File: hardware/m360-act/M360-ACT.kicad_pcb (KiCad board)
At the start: 2 copper layers, 100 x 80 mm, 30 parts, among them J1 5V do quadro, J2 M360-RF, J3 RJ45 RELES-A, J4 RJ45 RELES-B, J5 RJ45 SENSORES, SW1 Reed, U1 AMS1117-3.3, U2 74HCT244, U3 CD74HC4067, U4 SRV05-4, U5 SRV05-4, U6 SRV05-4, U7 SRV05-4, U8 SRV05-4

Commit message: feat(hardware): legendas de serigrafia na M360-LP e na M360-ACT
Serigrafia para quem monta e liga a placa, não só para quem a projetou.

**M360-ACT** — o campo Value dos conectores passa a aparecer na serigrafia: "5V do quadro",
"M360-RF", "RJ45 RELES-A", "RJ45 RELES-B" e "RJ45 SENSORES". Sem isso o instalador vê J3, J4 e
J5 e não tem como saber qual chicote vai onde. Mais o nome do modelo abaixo da marca.

**M360-LP** — nome do modelo abaixo da marca, e **VCC/GND nas ilhas do J3**. A entrada de
alimentação é um JST de 2 vias e nada na placa dizia qual é qual; ligar invertido queima o nó,
então a legenda é proteção, não conforto. A polaridade foi conferida na netlist, não deduzida da
ordem dos pinos: pino 1 = /VIN_RAW, pino 2 = GND (mesma rede de C4.2, C6.2, J1.8, J2.8).

Três armadilhas de serigrafia, todas custaram rodada extra e ficaram registradas no README:

- **o campo Value herda a rotação do footprint.** O J1 da ACT está em rot 90, e definir só a
  posição deixou "5V do quadro" na vertical, atravessando a própria ilha do borne
  (`silk_over_copper`). É preciso forçar o ângulo;
- **afastar um rótulo de uma ilha empurrando-o para a borda troca um problema por outro.** Ao
  tirar esse mesmo texto de cima da ilha, mandei-o para x = 99 — a placa começa em x = 100, e
  entraram um `silk_edge_clearance` e dois `silk_overlap`;
- **o DRC não pega tudo.** As legendas dos RJ45 na faixa de 2,5 mm entre os TVS e os conectores
  passavam no DRC e ficavam ilegíveis sobre os corpos. Só a inspeção da imagem mostrou; subiram
  para acima da fileira de TVS.

Verificação: LP com 8 violações e ACT com 13, todas `silk_edge_clearance` das frentes dos RJ45
rente à borda — intencionais e já registradas nos commits de roteamento. **0 itens desconectados
nas duas**, ou seja, nada de elétrico foi tocado.

Co-Authored-By: Claude Opus 5 (1M context) <noreply@anthropic.com>
Claude-Session: https://claude.ai/code/session_01G3CpSsqAsoKgMUYE5MhRV7
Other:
- board text added: "M360-ACT"
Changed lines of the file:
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@@
 		)
 		(property "Value" "RJ45 RELES-B"
-			(at 0 4.89 0)
-			(layer "F.Fab")
+			(at 0 -15.34 0)
+			(layer "F.SilkS")
 			(effects
 				(font
-					(size 1 1)
+					(size 0.9 0.9)
 					(thickness 0.15)
 				)
@@
 		)
 		(property "Value" "RJ45 RELES-A"
-			(at 0 4.89 0)
-			(layer "F.Fab")
+			(at 0 -15.34 0)
+			(layer "F.SilkS")
 			(effects
 				(font
-					(size 1 1)
+					(size 0.9 0.9)
 					(thickness 0.15)
 				)
@@
 		)
 		(property "Value" "M360-RF"
-			(at -1.27 12.93 0)
-			(layer "F.Fab")
+			(at 3.2 19.58 0)
+			(layer "F.SilkS")
 			(effects
 				(font
@@
 		)
 		(property "Value" "5V do quadro"
-			(at 0 4 90)
-			(layer "F.Fab")
+			(at -7.2 0 0)
+			(layer "F.SilkS")
 			(effects
 				(font
-					(size 1 1)
+					(size 0.8 0.8)
 					(thickness 0.15)
 				)
@@
 		)
 		(property "Value" "RJ45 SENSORES"
-			(at 0 4.89 0)
-			(layer "F.Fab")
+			(at 0 -15.34 0)
+			(layer "F.SilkS")
 			(effects
 				(font
-					(size 1 1)
+					(size 0.9 0.9)
 					(thickness 0.15)
 				)
@@
 		(layer "F.SilkS")
 		(effects
+			(font
+				(size 1.5 1.5)
+				(thickness 0.25)
+			)
+		)
+	)
+	(gr_text "M360-ACT"
+		(at 176 152 0)
+		(layer "F.SilkS")
+		(effects

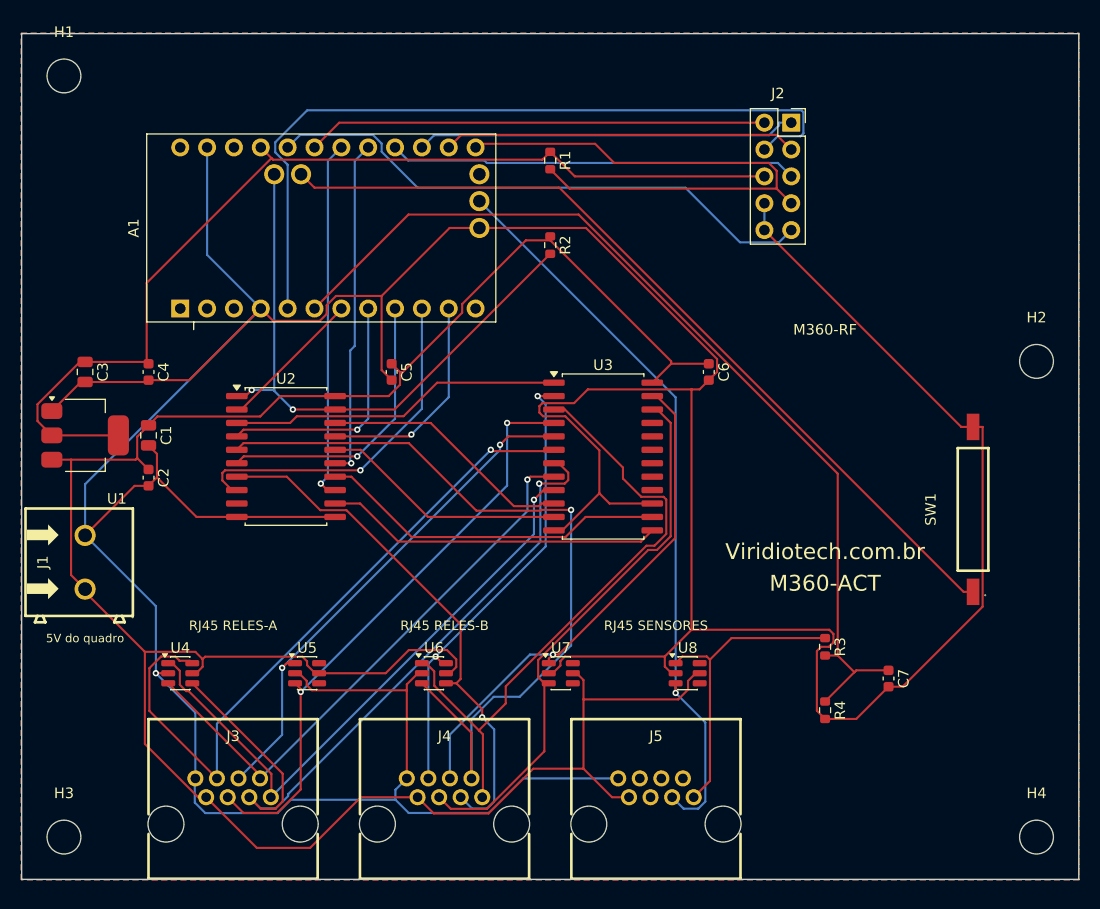
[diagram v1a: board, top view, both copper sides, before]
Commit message: feat(hardware): LP e ACT rerroteadas com o botão; GND volta a ser roteado
Conclui a troca do reed pelo botão iniciada em 0948368, que parou no esquemático.

Placas, para cada uma: del_fp.py SW1 → sincronização com o esquemático → place_*.py →
clear_tracks.py → export_dsn → dsn_sem_plano.py → Freerouting → import_ses →
zone_thermals.py → DRC com refill.

- M360-LP: 572 trilhas, 44 vias. DRC com 0 erros e 0 desconectados; restam os 8
  silk_edge_clearance dos RJ45, que já existiam.
- M360-ACT: 489 trilhas, 24 vias. DRC com 0 erros e 0 desconectados; restam os 13
  silk_edge_clearance, que já existiam. J1 em rot 0, como o place_act.py já pedia.
- Redes de todos os pads conferidas contra o HEAD: só o SW1 mudou. Trilhas todas de 0,25 mm.
- Paridade esquemático × placa com as mesmas contagens da base (237 e 195); some o
  footprint_symbol_mismatch do SW1.

**O GND não era roteado — e era isso que partia o plano.** Com zona de GND na placa, o DSN
declara `plane GND` e o Freerouting não desenha um fio de terra sequer. O primeiro roteamento
(bf701dc, 88 segmentos de GND) foi feito antes de as zonas existirem; todo rerroteamento
posterior perdia esse terra. Rerroteada com o DSN como sai do KiCad, a LP deu 16
unconnected_items, todos "Zona [GND]"; tirando as declarações plane, 0 — 100 segmentos de GND
na LP e 95 na ACT. Explica também os 15 desconectados imóveis da sessão anterior (§11.6).
Novo `tools/dsn_sem_plano.py`, e a §11 corrigida: 11.2, 11.4, 11.5 e 11.6.

Ajustes que o DRC pediu depois do rerroteamento:
- J4 da ACT, pino 8: starved_thermal → ligação sólida (pad_zone_connect.py), como o J3;
- silk_lp.py: referência do SW1 saía sobre "M360-LP"; vai para (172, 155);
- silk_act.py: referência do U1 encostava no J1, agora em rot 0; sobe para y = 143.

Botão: SHOU HAN TS665CJ, C393938, tátil 6 × 6 mm THT, SW1 nas três placas (LP, ACT e GW),
**solda manual e fora do PCBA**. Propriedade LCSC gravada nos três esquemáticos, com netlists
idênticas antes e depois. `add_lcsc.py` g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
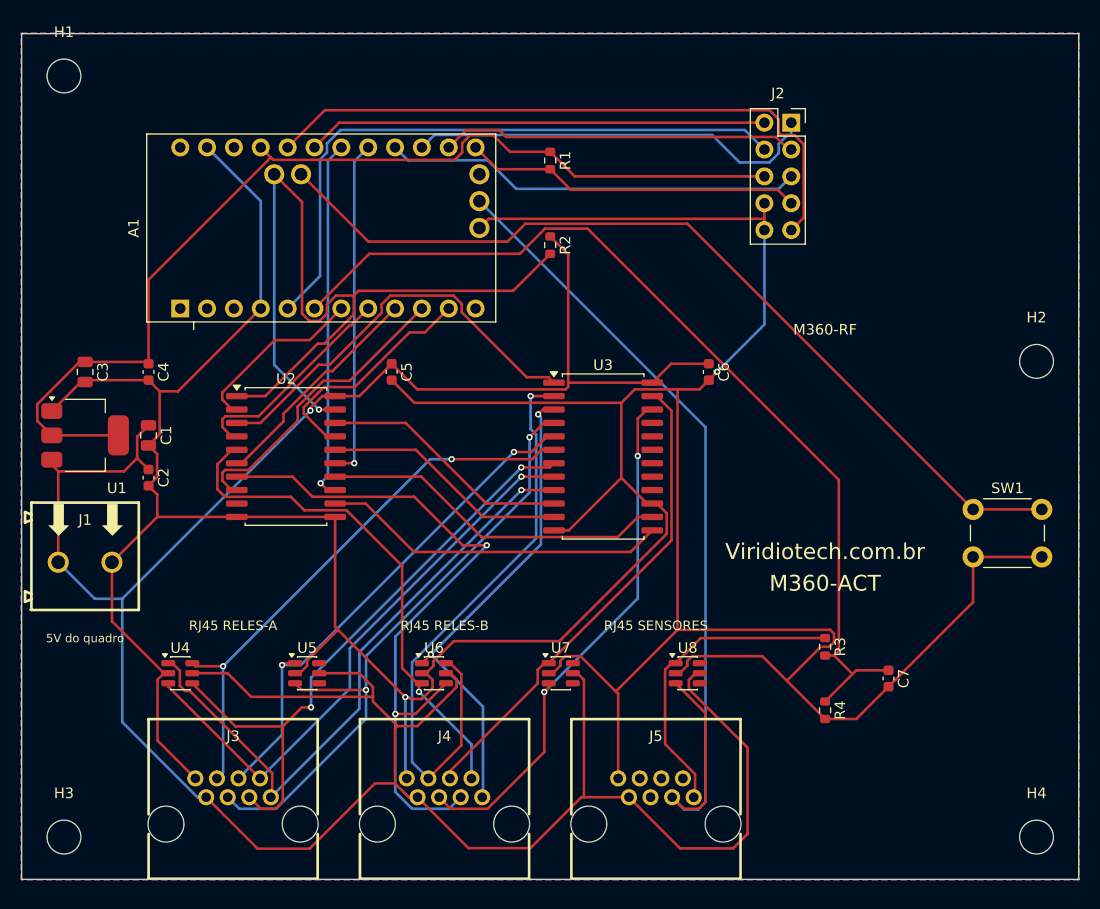
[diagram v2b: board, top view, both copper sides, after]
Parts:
- SW1: value Reed -> Repareamento; footprint M360:Reed_Littelfuse_59170 -> Button_Switch_THT:SW_PUSH_6mm
- turned J1 to 0 degrees
- turned SW1 to 0 degrees
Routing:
- net GND: track 432.9 -> 387.8 mm, vias 1 -> 2
- net +5V: track 226.8 -> 271.0 mm, vias 0 -> 1
- net REL_NFT: track 76.3 -> 48.4 mm
- net OE_N: track 57.2 -> 82.8 mm, vias 2 -> 1
- net NSS: track 55.5 -> 32.0 mm
- net REL_OXI: track 50.2 -> 66.5 mm, vias 1 -> 2
- net AUX_A6: track 70.4 -> 85.9 mm, vias 1 -> 0
- net REL_CH6: track 59.7 -> 45.6 mm, vias 0 -> 2
- net DIO0: track 73.8 -> 59.8 mm
- net REL_CH7: track 43.9 -> 57.1 mm, vias 2 -> 1
- net REL_CH3: track 65.7 -> 53.7 mm, vias 1 -> 2
- net REL_CH2: track 68.0 -> 58.9 mm, vias 1 -> 2
- net MUX_SIG: track 31.6 -> 39.3 mm
- net RF_RESET: track 53.3 -> 61.0 mm
- net MUX_S2_3V3: track 27.1 -> 21.5 mm, vias 1 -> 0
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
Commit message: feat(hardware): placa da M360-LP refeita sobre o esquemático corrigido
Sequência da §11.5: del_fp.py SW1 (botão → reed) → sincronização → place_lp.py →
clear_tracks.py → export_dsn (conferido: 61 peças, R25/R29 presentes, sem U8/J5, width 250,
0 fios) → dsn_sem_plano.py → Freerouting → import_ses → zone_thermals.py → silk_lp.py → DRC com
refill → pad_zone_connect.py J1 8 → solda_manual.py.

- Reed de volta em (160, 158); R26–R29 (100 Ω em série das digitais) numa fileira em y = 136,
  entre o TVS U5 e os pull-ups, mesmo passo e orientação destes. Sem sobreposição de courtyard.
- 606 trilhas de 0,25 mm e 47 vias; GND roteado (plano retirado do DSN).
- **DRC `--severity-all`: 0 violações e 0 pendências**, como pede o fluxo de hardware do
  projeto. Isso inclui os 8 `silk_edge_clearance` dos RJ45 que a placa carregava: eram a linha
  frontal, o fim das laterais e um círculo de 0,03 mm da serigrafia do footprint, colados na
  borda. Novo `tools/fix_rj45_silk.py` corrige a biblioteca e as cópias em todas as placas (a ACT
  recebe só esses 12 traços; continua defasada).
- `paridade.py`: idêntica ao esquemático. Arquivo de posição sem A1, J1–J4.
- Serigrafia: legenda "FTDI sem VCC" na faixa entre a borda e o Pro Mini; marca do pino 1 do
  soquete do mezanino; referência do U3 tirada de cima do "C9" (visto só no render 3D).

Documentação: status, §9 (placas defasadas: falta ACT e GW), §10, §11.4 e README das
ferramentas.

Co-Authored-By: Claude Opus 5 (1M context) <noreply@anthropic.com>
Claude-Session: https://claude.ai/code/session_012t7RkcrXvvpDVjKVimNu18
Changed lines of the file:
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@@
 		)
 		(fp_line
-			(start -8 8.6)
+			(start -8 8)
 			(end -8 4.36)
 			(stroke
@@
 		(fp_line
 			(start 8 4.36)
-			(end 8 8.6)
-			(stroke
-				(width 0.25)
-				(type solid)
-			)
-			(layer "F.SilkS")
-		)
-		(fp_line
-			(start 8 8.6)
-			(end -8 8.6)
+			(end 8 8)
 			(stroke
 				(width 0.25)
@@
 		)
 		(fp_circle
-			(center 8 8.62)
-			(end 8.03 8.62)
-			(stroke
-				(width 0.06)
-				(type solid)
-			)
-			(fill no)
-			(layer "F.SilkS")
-		)
-		(fp_circle
 			(center -6.35 3.43)
 			(end -5.55 3.43)
@@
 		)
 		(fp_line
-			(start -8 8.6)
+			(start -8 8)
 			(end -8 4.36)
 			(stroke
@@
 		(fp_line
 			(start 8 4.36)
-			(end 8 8.6)
-			(stroke
-				(width 0.25)
-				(type solid)
-			)
-			(layer "F.SilkS")
-		)
-		(fp_line
-			(start 8 8.6)
-			(end -8 8.6)
+			(end 8 8)
 			(stroke
 				(width 0.25)
@@
 		)
 		(fp_circle
-			(center 8 8.62)
-			(end 8.03 8.62)
-			(stroke
-				(width 0.06)
-				(type solid)
-			)
-			(fill no)
-			(layer "F.SilkS")
-		)
-		(fp_circle
 			(center -6.35 3.43)
 			(end -5.55 3.43)
@@
 		)
 		(fp_line
-			(start -8 8.6)
+			(start -8 8)
 			(end -8 4.36)
 			(stroke
@@
 		(fp_line
 			(start 8 4.36)
-			(end 8 8.6)
-			(stroke
-				(width 0.25)
-				(type solid)
-			)
-			(layer "F.SilkS")
-		)
-		(fp_line
-			(start 8 8.6)
-			(end -8 8.6)
+			(end 8 8)
 			(stroke
 				(width 0.25)
@@
 			(layer "F.SilkS")
 		)
-		(fp_circle
-			(center 8 8.62)
-			(end 8.03 8.62)
-			(stroke
-				(width 0.06)
-				(type solid)
-			)
-			(fill no)
-			(layer "F.SilkS")
-		)
